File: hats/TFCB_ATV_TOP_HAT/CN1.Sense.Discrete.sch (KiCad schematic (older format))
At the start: 42 parts

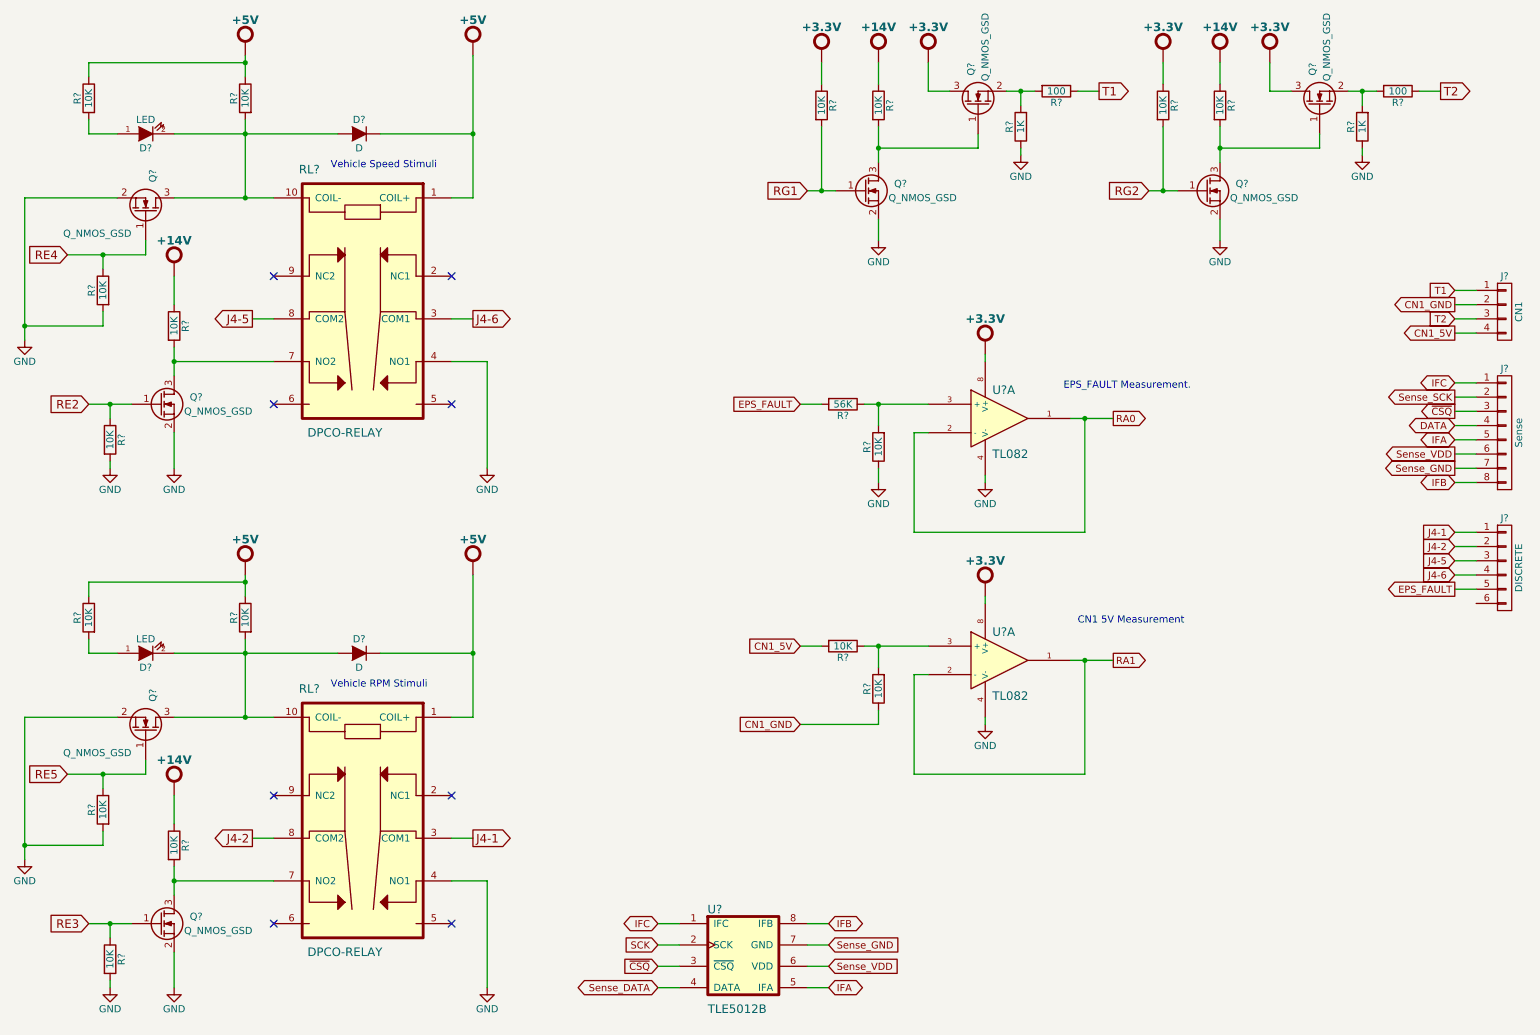
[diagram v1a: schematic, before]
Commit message: Added scanner trigger and current sense cct
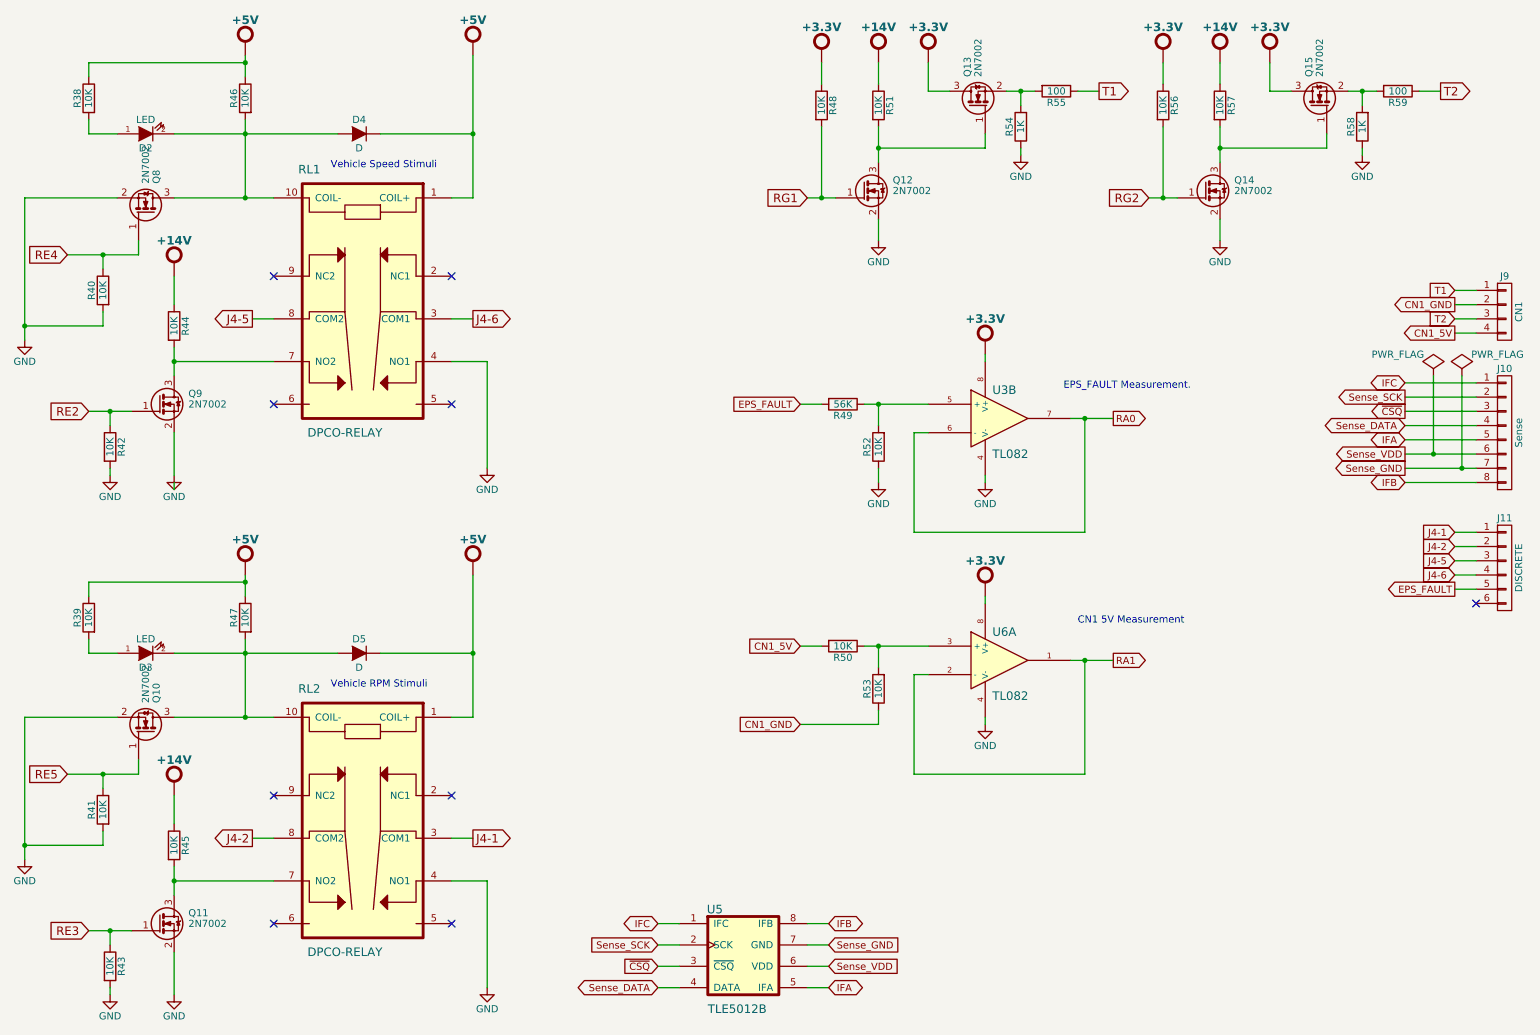
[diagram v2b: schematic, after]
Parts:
- removed Q? (x8): Q_NMOS_GSD, symbol Q_NMOS_GSD-RESCUE-TFCB_ATV_HAT
- added Q10, Q11, Q12, Q13, Q14, Q15, Q8, Q9: 2N7002, Housings_SOT-23_SOT-143_TSOT-6:SOT-23, symbol 2N7002
- D2, D3: renamed from D?; footprint (none) -> LEDs:LED-1206
- D4, D5: renamed from D?; footprint (none) -> Diodes_SMD:Diode-SMC_Handsoldering
- J10: renamed from J?; footprint (none) -> bjh-kicad-connector-fp:Weidmuller-SL-5.08-Vertical-8Pole
- J11: renamed from J?; footprint (none) -> bjh-kicad-connector-fp:Weidmuller-SL-5.08-Vertical-6Pole
- J9: renamed from J?; footprint (none) -> bjh-kicad-connector-fp:Weidmuller-SL-5.08-Vertical-4Pole
- R38, R39, R40, R41, R42, R43, R44, R45, R46, R47, R48, R49, R50, R51, R52, R53, R54, R55, R56, R57, R58, R59: renamed from R?; footprint (none) -> Resistors_SMD:R_0805_HandSoldering
- gave numbers to parts that had none: 5
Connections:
- net DATA is gone; now on net Sense_DATA: J10.4 (P4)
- net SCK is gone; now on net Sense_SCK: U5.2 (SCK)
- net +3.3V: now also Q13.3 (D), Q15.3 (D)
- net GND: now also Q10.2 (S), Q11.2 (S), Q12.2 (S), Q14.2 (S), Q8.2 (S), Q9.2 (S)
- net RA0: now also U3.6 (-), U3.7; no longer U3.1, U3.2 (-)
- net RE2: now also Q9.1 (G)
- net RE3: now also Q11.1 (G)
- net RE4: now also Q8.1 (G)
- net RE5: now also Q10.1 (G)
- net RG1: now also Q12.1 (G)
- net RG2: now also Q14.1 (G)
- net at R51.2: now also Q12.3 (D), Q13.1 (G)
- net at R54.2, R55.2: now also Q13.2 (S)
- net at R57.2: now also Q14.3 (D), Q15.1 (G)
- net at R58.2, R59.2: now also Q15.2 (S)
- net at D2.2 (K), D4.1 (A), R46.2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: now also Q8.3 (D)
- net at R44.2, RL1.7 (NO2): now also Q9.3 (D)
- net at R49.1, R52.2: now also U3.5 (+); no longer U3.3 (+)
- net at D3.2 (K), D5.1 (A), R47.2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: now also Q10.3 (D)
- net at R45.2, RL2.7 (NO2): now also Q11.3 (D)
- no-connect marks 8 -> 9
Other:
- moved on the sheet: R42, R43

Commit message: latest updates
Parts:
- RL1, RL2: footprint (none) -> bjh-kicad-switches-fp:EB2-5NU
- U3, U5, U6: footprint (none) -> Housings_SOIC:SOIC-8_3.9x4.9mm_Pitch1.27mm
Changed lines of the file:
@@
 F 0 "U5" H 5450 7050 60  0000 C CNN
 F 1 "TLE5012B" H 5400 6350 60  0000 L CNN
-F 2 "" H 5200 6950 60  0001 C CNN
+F 2 "Housings_SOIC:SOIC-8_3.9x4.9mm_Pitch1.27mm" H 5200 6950 60  0001 C CNN
 F 3 "" H 5200 6950 60  0000 C CNN
 	1    5200 6950
@@
 F 0 "U3" H 7400 3600 60  0000 L CNN
 F 1 "TL082" H 7400 3150 60  0000 L CNN
-F 2 "" H 7450 3400 60  0001 C CNN
+F 2 "Housings_SOIC:SOIC-8_3.9x4.9mm_Pitch1.27mm" H 7450 3400 60  0001 C CNN
 F 3 "" H 7450 3400 60  0000 C CNN
 	2    7450 3400
@@
 F 0 "U6" H 7400 5300 60  0000 L CNN
 F 1 "TL082" H 7400 4850 60  0000 L CNN
-F 2 "" H 7450 5100 60  0001 C CNN
+F 2 "Housings_SOIC:SOIC-8_3.9x4.9mm_Pitch1.27mm" H 7450 5100 60  0001 C CNN
 F 3 "" H 7450 5100 60  0000 C CNN
 	1    7450 5100
@@
 F 0 "RL1" H 2600 1850 60  0000 C CNN
 F 1 "DPCO-RELAY" H 2850 0   60  0000 C CNN
-F 2 "" V 3450 500 60  0001 C CNN
+F 2 "bjh-kicad-switches-fp:EB2-5NU" V 3450 500 60  0001 C CNN
 F 3 "" V 3450 500 60  0000 C CNN
 	1    2550 1750
@@
 F 0 "RL2" H 2600 5500 60  0000 C CNN
 F 1 "DPCO-RELAY" H 2850 3650 60  0000 C CNN
-F 2 "" V 3450 4150 60  0001 C CNN
+F 2 "bjh-kicad-switches-fp:EB2-5NU" V 3450 4150 60  0001 C CNN
 F 3 "" V 3450 4150 60  0000 C CNN
 	1    2550 5400

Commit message: More work on TFCB
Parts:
- removed D4, D5: D, Diodes_SMD:Diode-SMC_Handsoldering, symbol D-RESCUE-TFCB_ATV_HAT
- added D4, D5: D-BJH, symbol D-BJH
- renumbered U3 to U6
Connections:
- net +5V: now also D4.K, D5.K
- net RA0: now also U6.1, U6.2 (-); no longer U6.6 (-), U6.7
- net RA1: now also U6.6 (-), U6.7; no longer U6.1, U6.2 (-)
- net at D2.2 (K), Q8.3 (D), R46.2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: now also D4.A
- net at R49.1, R52.2: now also U6.3 (+); no longer U6.5 (+)
- net at R50.1, R53.2: now also U6.5 (+); no longer U6.3 (+)
- net at D3.2 (K), Q10.3 (D), R47.2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: now also D5.A
- net RE2 renamed RH4
- net RE3 renamed RJ6
- net RE4 renamed RH5
- net RE5 renamed RJ7
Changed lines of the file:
@@
 $EndComp
 $Comp
-L +14V_BJH #PWR056
+L +14V_BJH #PWR057
 U 1 1 558EB19F
 P 6600 850
-F 0 "#PWR056" H 6600 1040 20  0001 C CNN
+F 0 "#PWR057" H 6600 1040 20  0001 C CNN
 F 1 "+14V_BJH" H 6600 1040 51  0001 C CNN
 F 2 "" H 6600 850 60  0001 C CNN
@@
 $EndComp
 $Comp
-L +3.3V_BJH #PWR057
+L +3.3V_BJH #PWR058
 U 1 1 558EB293
 P 6950 850
-F 0 "#PWR057" H 6950 1040 20  0001 C CNN
+F 0 "#PWR058" H 6950 1040 20  0001 C CNN
 F 1 "+3.3V_BJH" H 6950 1040 51  0001 C CNN
 F 2 "" H 6950 850 60  0001 C CNN
@@
 T1
 $Comp
-L GND #PWR058
+L GND #PWR059
 U 1 1 558EB3B4
 P 6600 2150
-F 0 "#PWR058" H 6600 1900 50  0001 C CNN
+F 0 "#PWR059" H 6600 1900 50  0001 C CNN
 F 1 "GND" H 6600 2000 50  0000 C CNN
 F 2 "" H 6600 2150 60  0000 C CNN
@@
 $EndComp
 $Comp
-L +14V_BJH #PWR059
+L +14V_BJH #PWR060
 U 1 1 558EB78D
 P 9000 850
-F 0 "#PWR059" H 9000 1040 20  0001 C CNN
+F 0 "#PWR060" H 9000 1040 20  0001 C CNN
 F 1 "+14V_BJH" H 9000 1040 51  0001 C CNN
 F 2 "" H 9000 850 60  0001 C CNN
@@
 $EndComp
 $Comp
-L +3.3V_BJH #PWR060
+L +3.3V_BJH #PWR061
 U 1 1 558EB799
 P 9350 850
-F 0 "#PWR060" H 9350 1040 20  0001 C CNN
+F 0 "#PWR061" H 9350 1040 20  0001 C CNN
 F 1 "+3.3V_BJH" H 9350 1040 51  0001 C CNN
 F 2 "" H 9350 850 60  0001 C CNN
@@
 T2
 $Comp
-L GND #PWR061
+L GND #PWR062
 U 1 1 558EB7AA
 P 9000 2150
-F 0 "#PWR061" H 9000 1900 50  0001 C CNN
+F 0 "#PWR062" H 9000 1900 50  0001 C CNN
 F 1 "GND" H 9000 2000 50  0000 C CNN
 F 2 "" H 9000 2150 60  0000 C CNN
@@
 $EndComp
 $Comp
-L +3.3V_BJH #PWR062
+L +3.3V_BJH #PWR063
 U 1 1 558EC031
 P 6200 850
-F 0 "#PWR062" H 6200 1040 20  0001 C CNN
+F 0 "#PWR063" H 6200 1040 20  0001 C CNN
 F 1 "+3.3V_BJH" H 6200 1040 51  0001 C CNN
 F 2 "" H 6200 850 60  0001 C CNN
@@
 $EndComp
 $Comp
-L +3.3V_BJH #PWR063
+L +3.3V_BJH #PWR064
 U 1 1 558EC0D0
 P 8600 850
-F 0 "#PWR063" H 8600 1040 20  0001 C CNN
+F 0 "#PWR064" H 8600 1040 20  0001 C CNN
 F 1 "+3.3V_BJH" H 8600 1040 51  0001 C CNN
 F 2 "" H 8600 850 60  0001 C CNN
@@
 $EndComp
 $Comp
-L D-RESCUE-TFCB_ATV_HAT D?
-U 1 1 558ED8B2
-P 2950 1400
-AR Path="/558ED8B2" Ref="D?"  Part="1"
-AR Path="/558E7B4C/558ED8B2" Ref="D4"  Part="1"
-F 0 "D4" H 2950 1500 50  0000 C CNN
-F 1 "D" H 2950 1300 50  0000 C CNN
-F 2 "Diodes_SMD:Diode-SMC_Handsoldering" H 2950 1400 60  0001 C CNN
-F 3 "" H 2950 1400 60  0000 C CNN
-	1    2950 1400
-	1    0    0    -1
-$EndComp
-$Comp
-L +5V_BJH #PWR064
+L +5V_BJH #PWR065
 U 1 1 558EDA98
 P 2150 800
-F 0 "#PWR064" H 2150 990 20  0001 C CNN
+F 0 "#PWR065" H 2150 990 20  0001 C CNN
 F 1 "+5V_BJH" H 2150 990 51  0001 C CNN
 F 2 "" H 2150 800 60  0001 C CNN
@@
 $EndComp
 $Comp
-L +5V_BJH #PWR065
+L +5V_BJH #PWR066
 U 1 1 558EDF98
 P 3750 800
-F 0 "#PWR065" H 3750 990 20  0001 C CNN
+F 0 "#PWR066" H 3750 990 20  0001 C CNN
 F 1 "+5V_BJH" H 3750 990 51  0001 C CNN
 F 2 "" H 3750 800 60  0001 C CNN
@@
 $EndComp
 $Comp
-L GND #PWR066
+L GND #PWR067
 U 1 1 558EE53F
 P 1650 3800
-F 0 "#PWR066" H 1650 3550 50  0001 C CNN
+F 0 "#PWR067" H 1650 3550 50  0001 C CNN
 F 1 "GND" H 1650 3650 50  0000 C CNN
 F 2 "" H 1650 3800 60  0000 C CNN
@@
 $EndComp
 $Comp
-L GND #PWR067
+L GND #PWR068
 U 1 1 558EE5EE
 P 1200 3800
-F 0 "#PWR067" H 1200 3550 50  0001 C CNN
+F 0 "#PWR068" H 1200 3550 50  0001 C CNN
 F 1 "GND" H 1200 3650 50  0000 C CNN
 F 2 "" H 1200 3800 60  0000 C CNN
@@
 $EndComp
 $Comp
-L GND #PWR068
+L GND #PWR069
 U 1 1 558EE6AF
 P 3850 3750
-F 0 "#PWR068" H 3850 3500 50  0001 C CNN
+F 0 "#PWR069" H 3850 3500 50  0001 C CNN
 F 1 "GND" H 3850 3600 50  0000 C CNN
 F 2 "" H 3850 3750 60  0000 C CNN
@@
 $EndComp
 Text GLabel 900  2250 0    60   Input ~ 0
-RE4
+RH5
 $Comp
 L R R38
@@
 $EndComp
 $Comp
-L GND #PWR069
+L GND #PWR070
 U 1 1 558EECCB
 P 600 2850
-F 0 "#PWR069" H 600 2600 50  0001 C CNN
+F 0 "#PWR070" H 600 2600 50  0001 C CNN
 F 1 "GND" H 600 2700 50  0000 C CNN
 F 2 "" H 600 2850 60  0000 C CNN
@@
 NoConn ~ 2350 2400
 $Comp
-L +14V_BJH #PWR070
+L +14V_BJH #PWR071
 U 1 1 558EEF40
 P 1650 2350
-F 0 "#PWR070" H 1650 2540 20  0001 C CNN
+F 0 "#PWR071" H 1650 2540 20  0001 C CNN
 F 1 "+14V_BJH" H 1650 2540 51  0001 C CNN
 F 2 "" H 1650 2350 60  0001 C CNN
@@
 J4-5
 Text GLabel 1050 3350 0    60   Input ~ 0
-RE2
+RH4
 $Comp
 L R R54
@@
 $EndComp
 $Comp
-L GND #PWR071
+L GND #PWR072
 U 1 1 559B1D10
 P 7600 1550
-F 0 "#PWR071" H 7600 1300 50  0001 C CNN
+F 0 "#PWR072" H 7600 1300 50  0001 C CNN
 F 1 "GND" H 7600 1400 50  0000 C CNN
 F 2 "" H 7600 1550 60  0000 C CNN
@@
 $EndComp
 $Comp
-L GND #PWR072
+L GND #PWR073
 U 1 1 559B25E8
 P 10000 1550
-F 0 "#PWR072" H 10000 1300 50  0001 C CNN
+F 0 "#PWR073" H 10000 1300 50  0001 C CNN
 F 1 "GND" H 10000 1400 50  0000 C CNN
 F 2 "" H 10000 1550 60  0000 C CNN
@@
 EPS_FAULT
 $Comp
-L TL082 U3
-U 2 1 559C9903
+L TL082 U6
+U 1 1 559C9903
 P 7450 3400
-F 0 "U3" H 7400 3600 60  0000 L CNN
+F 0 "U6" H 7400 3600 60  0000 L CNN
 F 1 "TL082" H 7400 3150 60  0000 L CNN
 F 2 "Housings_SOIC:SOIC-8_3.9x4.9mm_Pitch1.27mm" H 7450 3400 60  0001 C CNN
 F 3 "" H 7450 3400 60  0000 C CNN
-	2    7450 3400
-	1    0    0    -1
-$EndComp
-$Comp
-L GND #PWR073
+	1    7450 3400
+	1    0    0    -1
+$EndComp
+$Comp
+L GND #PWR074
 U 1 1 559C9912
 P 7350 3850
-F 0 "#PWR073" H 7350 3600 50  0001 C CNN
+F 0 "#PWR074" H 7350 3600 50  0001 C CNN
 F 1 "GND" H 7350 3700 50  0000 C CNN
 F 2 "" H 7350 3850 60  0000 C CNN
@@
 $EndComp
 $Comp
-L GND #PWR074
+L GND #PWR075
 U 1 1 559C9943
 P 6600 3850
-F 0 "#PWR074" H 6600 3600 50  0001 C CNN
+F 0 "#PWR075" H 6600 3600 50  0001 C CNN
 F 1 "GND" H 6600 3700 50  0000 C CNN
 F 2 "" H 6600 3850 60  0000 C CNN
@@
 RA0
 $Comp
-L +3.3V_BJH #PWR075
+L +3.3V_BJH #PWR076
 U 1 1 559C9E02
 P 7350 2900
-F 0 "#PWR075" H 7350 3090 20  0001 C CNN
+F 0 "#PWR076" H 7350 3090 20  0001 C CNN
 F 1 "+3.3V_BJH" H 7350 3090 51  0001 C CNN
 F 2 "" H 7350 2900 60  0001 C CNN
@@
 $Comp
 L TL082 U6
-U 1 1 559CBF14
+U 2 1 559CBF14
 P 7450 5100
 F 0 "U6" H 7400 5300 60  0000 L CNN
@@
 F 2 "Housings_SOIC:SOIC-8_3.9x4.9mm_Pitch1.27mm" H 7450 5100 60  0001 C CNN
 F 3 "" H 7450 5100 60  0000 C CNN
-	1    7450 5100
-	1    0    0    -1
-$EndComp
-$Comp
-L GND #PWR076
+	2    7450 5100
+	1    0    0    -1
+$EndComp
+$Comp
+L GND #PWR077
 U 1 1 559CBF1A
 P 7350 5550
-F 0 "#PWR076" H 7350 5300 50  0001 C CNN
+F 0 "#PWR077" H 7350 5300 50  0001 C CNN
 F 1 "GND" H 7350 5400 50  0000 C CNN
 F 2 "" H 7350 5550 60  0000 C CNN
@@
 RA1
 $Comp
-L +3.3V_BJH #PWR077
+L +3.3V_BJH #PWR078
 U 1 1 559CBF40
 P 7350 4600
-F 0 "#PWR077" H 7350 4790 20  0001 C CNN
+F 0 "#PWR078" H 7350 4790 20  0001 C CNN
 F 1 "+3.3V_BJH" H 7350 4790 51  0001 C CNN
 F 2 "" H 7350 4600 60  0001 C CNN
@@
 $EndComp
 $Comp
-L D-RESCUE-TFCB_ATV_HAT D5
-U 1 1 55A50EC6
-P 2950 5050
-F 0 "D5" H 2950 5150 50  0000 C CNN
-F 1 "D" H 2950 4950 50  0000 C CNN
-F 2 "Diodes_SMD:Diode-SMC_Handsoldering" H 2950 5050 60  0001 C CNN
-F 3 "" H 2950 5050 60  0000 C CNN
-	1    2950 5050
-	1    0    0    -1
-$EndComp
-$Comp
-L +5V_BJH #PWR078
+L +5V_BJH #PWR079
 U 1 1 55A50ED3
 P 2150 4450
-F 0 "#PWR078" H 2150 4640 20  0001 C CNN
+F 0 "#PWR079" H 2150 4640 20  0001 C CNN
 F 1 "+5V_BJH" H 2150 4640 51  0001 C CNN
 F 2 "" H 2150 4450 60  0001 C CNN
@@
 $EndComp
 $Comp
-L +5V_BJH #PWR079
+L +5V_BJH #PWR080
 U 1 1 55A50EDA
 P 3750 4450
-F 0 "#PWR079" H 3750 4640 20  0001 C CNN
+F 0 "#PWR080" H 3750 4640 20  0001 C CNN
 F 1 "+5V_BJH" H 3750 4640 51  0001 C CNN
 F 2 "" H 3750 4450 60  0001 C CNN
@@
 $EndComp
 $Comp
-L GND #PWR080
+L GND #PWR081
 U 1 1 55A50EF2
 P 1650 7450
-F 0 "#PWR080" H 1650 7200 50  0001 C CNN
+F 0 "#PWR081" H 1650 7200 50  0001 C CNN
 F 1 "GND" H 1650 7300 50  0000 C CNN
 F 2 "" H 1650 7450 60  0000 C CNN
@@
 $EndComp
 $Comp
-L GND #PWR081
+L GND #PWR082
 U 1 1 55A50EF8
 P 1200 7450
-F 0 "#PWR081" H 1200 7200 50  0001 C CNN
+F 0 "#PWR082" H 1200 7200 50  0001 C CNN
 F 1 "GND" H 1200 7300 50  0000 C CNN
 F 2 "" H 1200 7450 60  0000 C CNN
@@
 $EndComp
 $Comp
-L GND #PWR082
+L GND #PWR083
 U 1 1 55A50EFE
 P 3850 7400
-F 0 "#PWR082" H 3850 7150 50  0001 C CNN
+F 0 "#PWR083" H 3850 7150 50  0001 C CNN
 F 1 "GND" H 3850 7250 50  0000 C CNN
 F 2 "" H 3850 7400 60  0000 C CNN
@@
 $EndComp
 Text GLabel 900  5900 0    60   Input ~ 0
-RE5
+RJ7
 $Comp
 L R R39
@@
 $EndComp
 $Comp
-L GND #PWR083
+L GND #PWR084
 U 1 1 55A50F17
 P 600 6500
-F 0 "#PWR083" H 600 6250 50  0001 C CNN
+F 0 "#PWR084" H 600 6250 50  0001 C CNN
 F 1 "GND" H 600 6350 50  0000 C CNN
 F 2 "" H 600 6500 60  0000 C CNN
@@
 NoConn ~ 2350 6050
 $Comp
-L +14V_BJH #PWR084
+L +14V_BJH #PWR085
 U 1 1 55A50F20
 P 1650 6000
-F 0 "#PWR084" H 1650 6190 20  0001 C CNN
+F 0 "#PWR085" H 1650 6190 20  0001 C CNN
 F 1 "+14V_BJH" H 1650 6190 51  0001 C CNN
 F 2 "" H 1650 6000 60  0001 C CNN
@@
 J4-2
 Text GLabel 1050 7000 0    60   Input ~ 0
-RE3
+RJ6
 Text Notes 2750 5300 0    50   ~ 0
 Vehicle RPM Stimuli
@@
 NoConn ~ 10800 4700
 $Comp
-L PWR_FLAG #FLG085
+L PWR_FLAG #FLG086
 U 1 1 55B00CA3
 P 10500 3100
-F 0 "#FLG085" H 10500 3195 50  0001 C CNN
+F 0 "#FLG086" H 10500 3195 50  0001 C CNN
 F 1 "PWR_FLAG" H 10250 3250 50  0000 C CNN
 F 2 "" H 10500 3100 60  0000 C CNN
@@
 $EndComp
 $Comp
-L PWR_FLAG #FLG086
+L PWR_FLAG #FLG087
 U 1 1 55B014EA
 P 10700 3100
-F 0 "#FLG086" H 10700 3195 50  0001 C CNN
+F 0 "#FLG087" H 10700 3195 50  0001 C CNN
 F 1 "PWR_FLAG" H 10950 3250 50  0000 C CNN
 F 2 "" H 10700 3100 60  0000 C CNN
@@
 Wire Wire Line
 	9750 1500 9750 1400
+$Comp
+L D-BJH D4
+U 1 1 55C4AD6F
+P 2950 1400
+F 0 "D4" H 2950 1500 50  0000 C CNN
+F 1 "D-BJH" H 2950 1300 50  0001 C CNN
+F 2 "" H 2950 1400 60  0000 C CNN
+F 3 "" H 2950 1400 60  0000 C CNN
+	1    2950 1400
+	-1   0    0    1
+$EndComp
+$Comp
+L D-BJH D5
+U 1 1 55C4B020
+P 2950 5050
+F 0 "D5" H 2950 5150 50  0000 C CNN
+F 1 "D-BJH" H 2950 4950 50  0001 C CNN
+F 2 "" H 2950 5050 60  0000 C CNN
+F 3 "" H 2950 5050 60  0000 C CNN
+	1    2950 5050
+	-1   0    0    1
+$EndComp
 $EndSCHEMATC
